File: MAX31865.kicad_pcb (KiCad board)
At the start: 2 copper layers, 25.4 x 27.9 mm, 23 parts, among them J1 connector, J2 Screw_Terminal_01x04, U1 MAX31865, U2 MIC5225

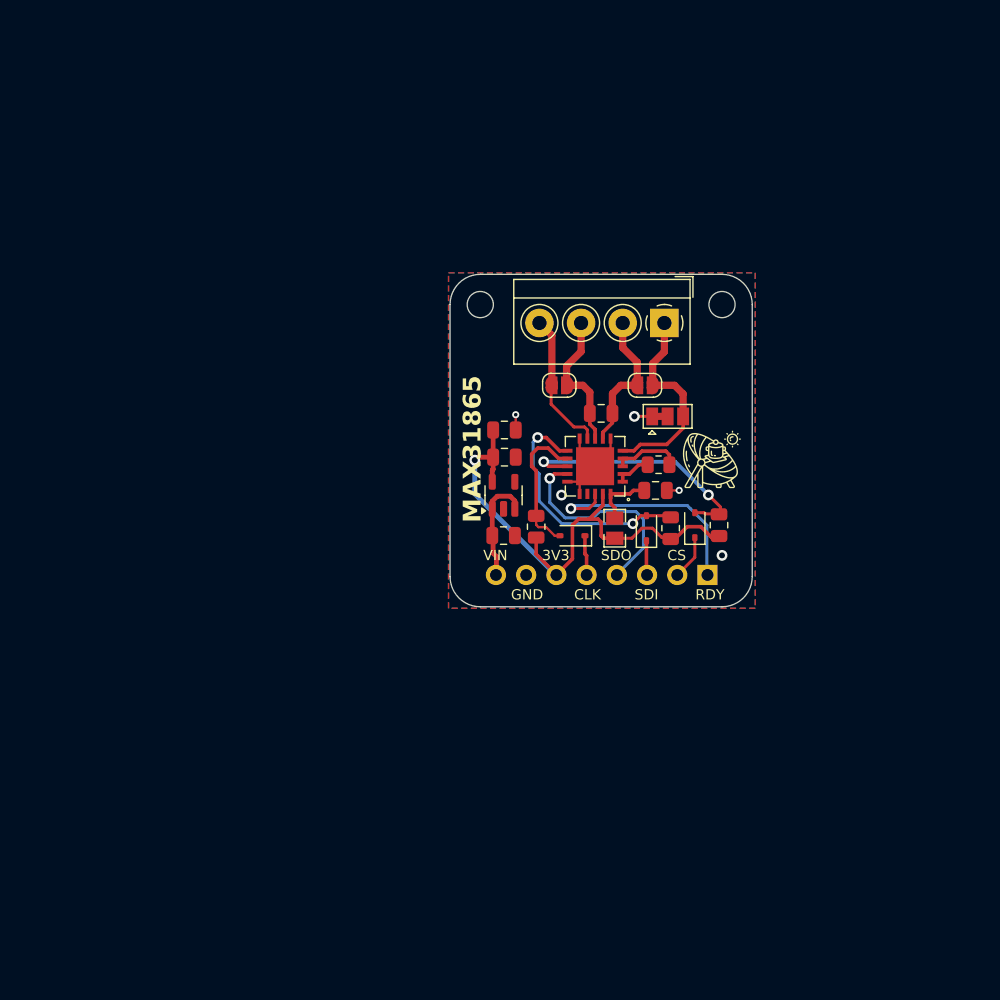
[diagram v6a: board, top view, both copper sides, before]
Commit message: Updated AFE with Arduino shield
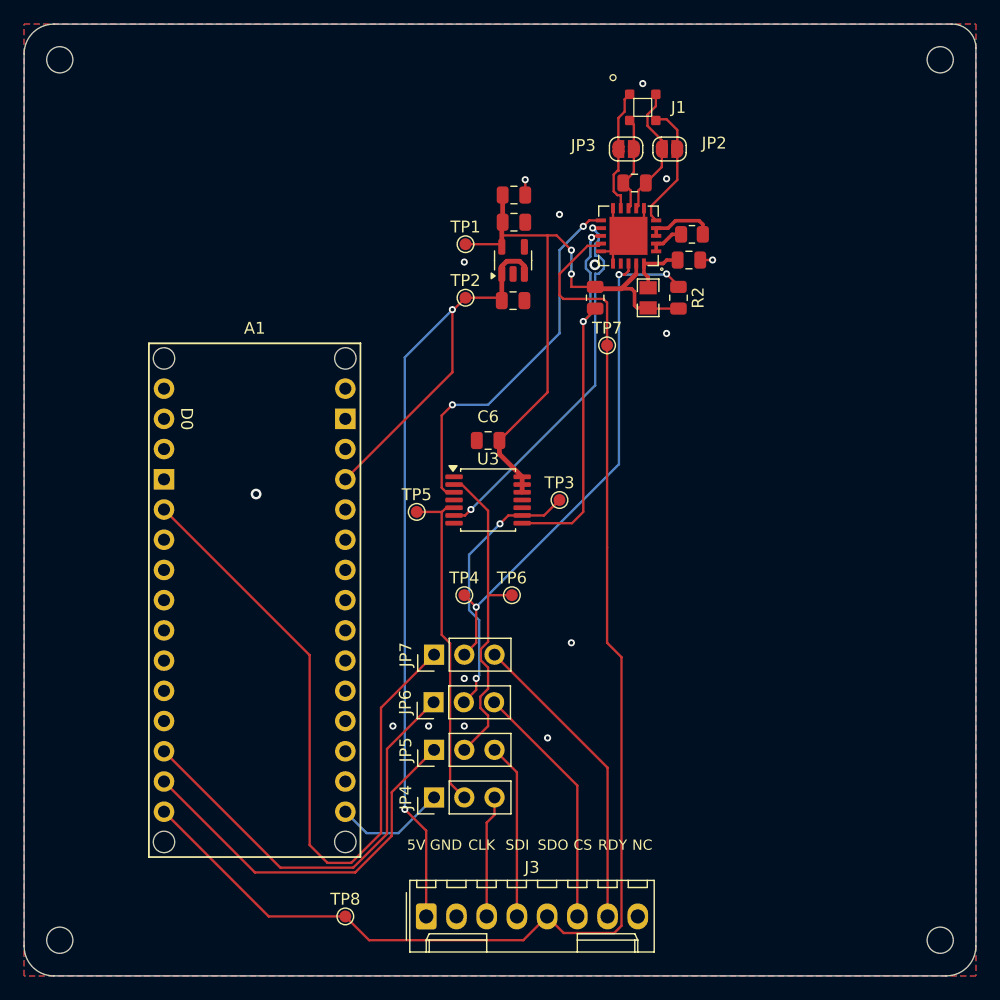
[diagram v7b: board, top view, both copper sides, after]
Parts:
- removed D1, D2, D3: 1N4148, Diode_SMD:D_SOD-323
- removed G***: LOGO, external_footprints:logo
- removed J2: Screw_Terminal_01x04, TerminalBlock_4Ucon:TerminalBlock_4Ucon_1x04_P3.50mm_Horizontal
- removed JP1: SolderJumper_3_Bridged12, Jumper:SolderJumper-3_P1.3mm_Bridged12_Pad1.0x1.5mm
- removed R6, R7: 10K, Resistor_SMD:R_0805_2012Metric
- added A1: Arduino_Nano_Socket, PCM_arduino-library:Arduino_Nano_Socket, F.Cu at (119.4, 140.0)
- added C6: 0.1uF, Capacitor_SMD:C_0805_2012Metric, F.Cu at (139.0, 105.0)
- added J3: Conn_01x08, Connector_Molex:Molex_KK-254_AE-6410-08A_1x08_P2.54mm_Vertical, F.Cu at (133.8, 145.0)
- added JP4: Jumper_3_Open, Connector_PinHeader_2.54mm:PinHeader_1x03_P2.54mm_Vertical, F.Cu at (134.5, 135.0)
- added JP5: Jumper_3_Open, Connector_PinHeader_2.54mm:PinHeader_1x03_P2.54mm_Vertical, F.Cu at (134.5, 131.0)
- added JP6: Jumper_3_Open, Connector_PinHeader_2.54mm:PinHeader_1x03_P2.54mm_Vertical, F.Cu at (134.4, 127.0)
- added JP7: Jumper_3_Open, Connector_PinHeader_2.54mm:PinHeader_1x03_P2.54mm_Vertical, F.Cu at (134.5, 123.0)
- added R2: 10K, Resistor_SMD:R_0805_2012Metric, F.Cu at (155.0, 93.0)
- added TP1: TestPoint, TestPoint:TestPoint_Pad_D1.0mm, F.Cu at (137.1, 88.5)
- added TP2: TestPoint, TestPoint:TestPoint_Pad_D1.0mm, F.Cu at (137.1, 93.0)
- added TP3: TestPoint, TestPoint:TestPoint_Pad_D1.0mm, F.Cu at (145.0, 110.0)
- added TP4: TestPoint, TestPoint:TestPoint_Pad_D1.0mm, F.Cu at (137.0, 118.0)
- added TP5: TestPoint, TestPoint:TestPoint_Pad_D1.0mm, F.Cu at (133.0, 111.0)
- added TP6: TestPoint, TestPoint:TestPoint_Pad_D1.0mm, F.Cu at (141.0, 118.0)
- added TP7: TestPoint, TestPoint:TestPoint_Pad_D1.0mm, F.Cu at (149.0, 97.0)
- added TP8: TestPoint, TestPoint:TestPoint_Pad_D1.0mm, F.Cu at (127.0, 145.0)
- added U$1: MOUNTINGHOLE2.5, MountingHole:MountingHole_2.2mm_M2_ISO7380, F.Cu at (177.0, 147.0)
- added U$2: MOUNTINGHOLE2.5, MountingHole:MountingHole_2.2mm_M2_ISO7380, F.Cu at (103.0, 147.0)
- added U3: 74LVC125, Package_SO:TSSOP-14_4.4x5mm_P0.65mm, F.Cu at (139.0, 110.0)
- J1: value connector -> Conn_01x04; footprint Connector_PinHeader_2.54mm:PinHeader_1x08_P2.54mm_Vertical -> SensorFootprint:RTD_Sensor_BondPad_4x; moved to F.Cu
- moved U$18 40.9 mm to (103.0, 73.0)
- moved J1 39.7 mm to (152.0, 77.0), turned to 0 degrees
- moved U$19 27.6 mm to (177.0, 73.0)
- moved JP3 20.6 mm to (150.6, 80.5)
- moved JP2 20.0 mm to (154.2, 80.5)
- moved R8 19.9 mm to (148.0, 93.0), turned to 90 degrees
- moved C1 19.8 mm to (141.2, 84.4)
- moved C5 19.8 mm to (141.2, 86.7)
- moved U2 19.8 mm to (141.1, 89.9)
- moved C4 19.8 mm to (141.1, 93.2)
- moved U1 19.6 mm to (150.8, 87.8)
- moved C2 19.6 mm to (155.9, 89.8)
- moved C3 19.6 mm to (151.3, 83.4)
- moved FB1 19.6 mm to (152.5, 93.0)
- moved R1 19.6 mm to (156.1, 87.7)
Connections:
- C1 pad 1: VDD -> 3V3
- C3 pad 1: Net-(J2-Pin_2) -> /SENSOR_S+
- C3 pad 2: Net-(J2-Pin_3) -> /SENSOR_S-
- C4 pad 1: VIN -> 5V
- C5 pad 1: VDD -> 3V3
- FB1 pad 2: VDD -> 3V3
- J1 pad 1: /DRDY -> /SENSOR_F-
- J1 pad 2: /CS_5V -> /SENSOR_S+
- J1 pad 3: /SDI_5V -> /SENSOR_S-
- J1 pad 4: /SDO -> /SENSOR_F+
- JP2 pad 1: Net-(J2-Pin_2) -> /SENSOR_S+
- JP2 pad 2: Net-(J2-Pin_1) -> /SENSOR_F+
- JP3 pad 1: Net-(J2-Pin_4) -> /SENSOR_F-
- JP3 pad 2: Net-(J2-Pin_3) -> /SENSOR_S-
- R8 pad 1: Net-(D2-A) -> /CS
- R8 pad 2: VDD -> 3V3
- U1 pad 11: Net-(D1-A) -> /SDI
- U1 pad 12: Net-(D2-A) -> /SCLK
- U1 pad 13: Net-(D3-A) -> /CS
- U1 pad 18: /DRDY -> /DRDY_JP
- U1 pad 19: VDD -> 3V3
- U1 pad 5: Net-(J2-Pin_1) -> /SENSOR_F+
- U1 pad 7: Net-(J2-Pin_2) -> /SENSOR_S+
- U1 pad 8: Net-(J2-Pin_3) -> /SENSOR_S-
- U1 pad 9: Net-(J2-Pin_4) -> /SENSOR_F-
- U2 pad 1: VIN -> 5V
- U2 pad 3: VIN -> 5V
- U2 pad 5: VDD -> 3V3
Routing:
- net /SDO: track 18.7 -> 108.0 mm, vias 1 -> 0
- net 5V: track 0.00 -> 81.9 mm, vias 0 -> 2
- net 3V3: track 0.00 -> 55.0 mm, vias 0 -> 2
- net /DRDY_JP: track 0.00 -> 45.8 mm, vias 0 -> 3
- net VDD: track 45.6 -> 0.00 mm, vias 1 -> 0
- net /DRDY: track 19.4 -> 57.8 mm, vias 1 -> 0
- net /CS_5V: track 3.75 -> 36.7 mm
- net /MOSI_5V: track 0.00 -> 32.3 mm
- net /CS: track 0.00 -> 31.7 mm, vias 0 -> 2
- net /SCLK: track 0.00 -> 31.6 mm, vias 0 -> 2
- net /SDI: track 0.00 -> 31.5 mm, vias 0 -> 2
- net /SCK_JP: track 0.00 -> 28.1 mm
- net /MOSI_JP: track 0.00 -> 27.7 mm
- net /DRDY_EXT: track 0.00 -> 25.9 mm
- net /CS_JP: track 0.00 -> 22.8 mm, vias 0 -> 2
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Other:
- board size 25.4 x 27.9 mm -> 80 x 80 mm
- board text added: "5V"
- board text added: "NC"
- board text removed: "3V3"
- board text removed: "MAX31865"
- board text removed: "VIN"

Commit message: Updated layout
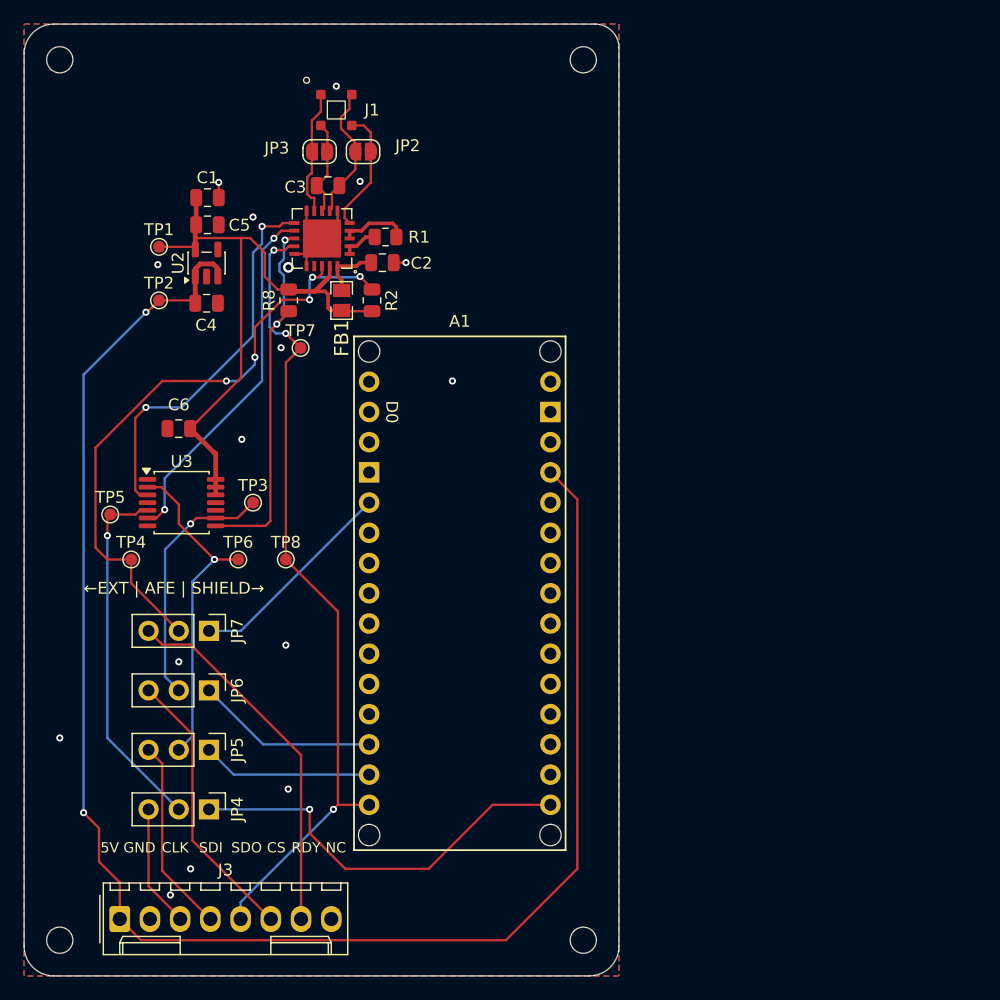
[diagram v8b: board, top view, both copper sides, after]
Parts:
- moved TP8 30.4 mm to (122.0, 115.0)
- moved U$1 30.0 mm to (147.0, 147.0)
- moved U$19 30.0 mm to (147.0, 73.0)
- moved TP4 28.2 mm to (109.0, 115.0)
- moved C6 26.0 mm to (113.0, 104.0)
- moved C1 25.8 mm to (115.4, 84.6)
- moved C5 25.8 mm to (115.4, 86.9)
- moved J1 25.8 mm to (126.2, 77.2)
- moved J3 25.8 mm to (108.0, 145.2)
- moved R8 25.8 mm to (122.2, 93.2)
- moved TP3 25.8 mm to (119.2, 110.2)
- moved TP5 25.8 mm to (107.2, 111.2)
- moved TP7 25.8 mm to (123.2, 97.2)
- moved U1 25.8 mm to (125.0, 88.0)
- moved U3 25.8 mm to (113.2, 110.2)
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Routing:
- net 5V: track 81.9 -> 140.8 mm
- net /SDO: track 108.0 -> 68.1 mm, vias 0 -> 3
- net /DRDY: track 57.8 -> 17.9 mm
- net /SCK_5V: track 9.45 -> 34.2 mm, vias 0 -> 1
- net /CS_5V: track 36.7 -> 15.3 mm
- net /MOSI_5V: track 32.3 -> 14.3 mm
- net /DRDY_JP: track 45.8 -> 53.5 mm, vias 3 -> 5
- net /DRDY_EXT: track 25.9 -> 30.9 mm
- net /SCK_JP: track 28.1 -> 30.7 mm, vias 0 -> 1
- net /CS_EXT: track 20.9 -> 23.5 mm
- net /MOSI_EXT: track 14.8 -> 16.4 mm
- net /CS_JP: track 22.8 -> 21.3 mm, vias 2 -> 1
- net /SCLK: track 31.6 -> 30.3 mm
- net /SDI: track 31.5 -> 32.4 mm
- net /MOSI_JP: track 27.7 -> 28.3 mm, vias 0 -> 1
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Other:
- board size 80 x 80 mm -> 50 x 80 mm
- board text added: "←EXT | AFE | SHIELD→"
